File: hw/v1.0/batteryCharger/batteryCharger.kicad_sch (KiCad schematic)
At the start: 27 parts, among them J1 PWR_IN, J2 USB_B_Micro, J3 USB_C_Receptacle_USB2.0, J4 BAT+, J5 BAT-, U1 LT3652EMSE

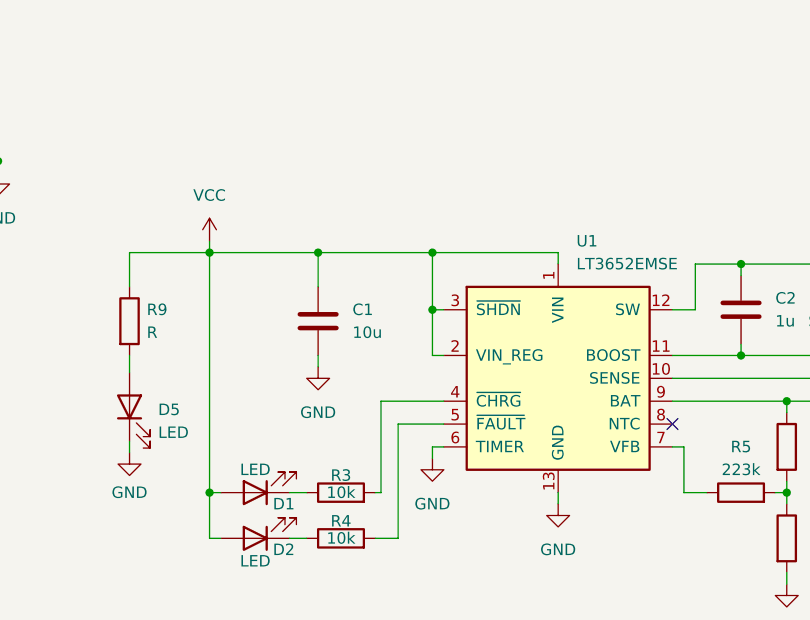
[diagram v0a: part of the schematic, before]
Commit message: Tweak silkscreen at mainBoard, add MPPT option to batteryCharger
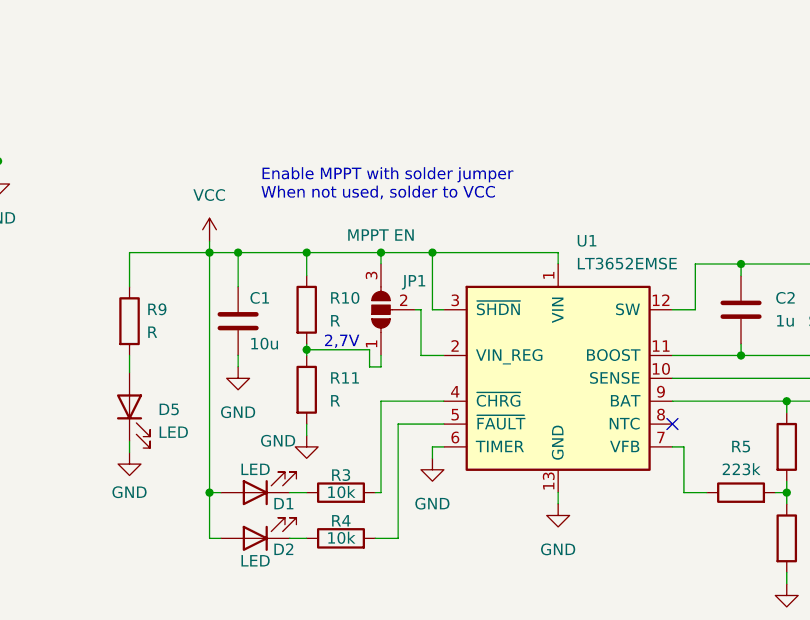
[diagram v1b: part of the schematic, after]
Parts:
- added JP1: MPPT EN, Jumper:SolderJumper-3_P1.3mm_Open_RoundedPad1.0x1.5mm_NumberLabels, symbol Jumper:SolderJumper_3_Open
- added R10, R11: R, Resistor_SMD:R_0805_2012Metric_Pad1.20x1.40mm_HandSolder, symbol Device:R
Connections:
- net GND: now also R11.2
- net VCC: now also JP1.3 (B), R10.1; no longer U1.2 (VIN_REG)
- new net: JP1.1 (A), R10.2, R11.1
- new net: JP1.2 (C), U1.2 (VIN_REG)
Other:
- note added: "2,7V"
- note added: "Enable MPPT with solder jumper When not used, solder to VCC"
- moved on the sheet: C1

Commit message: Inlcude schematics in text
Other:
- company: (none) -> Martin Kousal
- title: (none) -> batteryCharger
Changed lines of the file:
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@@
 (kicad_sch (version 20211123) (generator eeschema)
   (paper "A4")
+  (title_block
+    (title "batteryCharger")
+    (date "3.04.2022")
+    (rev "v1.0")
+    (company "Martin Kousal")
+  )
   (junction (at 48.26 125.095) (diameter 0) (color 0 0 0 0)
   )
